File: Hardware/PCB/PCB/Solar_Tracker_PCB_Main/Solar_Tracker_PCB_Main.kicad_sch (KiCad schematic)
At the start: 1 part, among them J1 MTJ-88ARX1-FSM-LG

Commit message: Colocacion de los componentes en el PCB
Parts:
- removed J1: MTJ-88ARX1-FSM-LG, MTJ-88ARX1:MTJ88ARX1FSMLG, symbol MTJ-88ARX1-FSM-LG:MTJ-88ARX1-FSM-LG
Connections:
- no-connect marks 14 -> 0
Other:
- note removed: "RJ45 FEMALE"
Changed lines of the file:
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@@
 	(generator_version "9.0")
 	(paper "A4")
-	(rectangle
-		(start 236.22 12.7)
-		(end 284.48 59.69)
-		(stroke
-			(width 0)
-			(type default)
-		)
-		(fill
-			(type none)
-		)
-	)
-	(text "RJ45 FEMALE"
-		(exclude_from_sim no)
-		(at 260.35 20.32 0)
-		(effects
-			(font
-				(size 1.27 1.27)
-			)
-		)
-	)
-	(no_connect
-		(at 248.92 38.1)
-	)
-	(no_connect
-		(at 271.78 33.02)
-	)
-	(no_connect
-		(at 248.92 35.56)
-	)
-	(no_connect
-		(at 248.92 48.26)
-	)
-	(no_connect
-		(at 271.78 38.1)
-	)
-	(no_connect
-		(at 248.92 43.18)
-	)
-	(no_connect
-		(at 271.78 40.64)
-	)
-	(no_connect
-		(at 271.78 35.56)
-	)
-	(no_connect
-		(at 248.92 33.02)
-	)
-	(no_connect
-		(at 271.78 48.26)
-	)
-	(no_connect
-		(at 271.78 45.72)
-	)
-	(no_connect
-		(at 248.92 40.64)
-	)
-	(no_connect
-		(at 248.92 45.72)
-	)
-	(no_connect
-		(at 271.78 43.18)
-	)
-	(symbol
-		(lib_id "MTJ-88ARX1-FSM-LG:MTJ-88ARX1-FSM-LG")
-		(at 248.92 33.02 0)
-		(unit 1)
-		(exclude_from_sim no)
-		(in_bom yes)
-		(on_board yes)
-		(dnp no)
-		(fields_autoplaced yes)
-		(property "Reference" "J1"
-			(at 260.35 25.4 0)
-			(effects
-				(font
-					(size 1.27 1.27)
-				)
-			)
-		)
-		(property "Value" "MTJ-88ARX1-FSM-LG"
-			(at 260.35 27.94 0)
-			(effects
-				(font
-					(size 1.27 1.27)
-				)
-			)
-		)
-		(property "Footprint" "MTJ-88ARX1:MTJ88ARX1FSMLG"
-			(at 267.97 127.94 0)
-			(effects
-				(font
-					(size 1.27 1.27)
-				)
-				(justify left top)
-				(hide yes)
-			)
-		)
-		(property "Datasheet" "https://www.arrow.com/en/products/mtj-88arx1-fsm-lg/adam-tech"
-			(at 267.97 227.94 0)
-			(effects
-				(font
-					(size 1.27 1.27)
-				)
-				(justify left top)
-				(hide yes)
-			)
-		)
-		(property "Description" "RJ45 Modular Jack, Shielded, Dip, Side Entry,LEDs"
-			(at 248.92 33.02 0)
-			(effects
-				(font
-					(size 1.27 1.27)
-				)
-				(hide yes)
-			)
-		)
-		(property "Height" "13.708"
-			(at 267.97 427.94 0)
-			(effects
-				(font
-					(size 1.27 1.27)
-				)
-				(justify left top)
-				(hide yes)
-			)
-		)
-		(property "Mouser Part Number" "737-MTJ88ARX1FSMLG"
-			(at 267.97 527.94 0)
-			(effects
-				(font
-					(size 1.27 1.27)
-				)
-				(justify left top)
-				(hide yes)
-			)
-		)
-		(property "Mouser Price/Stock" "https://www.mouser.co.uk/ProductDetail/Adam-Tech/MTJ-88ARX1-FSM-LG?qs=HoCaDK9Nz5cwcndn7zcdzQ%3D%3D"
-			(at 267.97 627.94 0)
-			(effects
-				(font
-					(size 1.27 1.27)
-				)
-				(justify left top)
-				(hide yes)
-			)
-		)
-		(property "Manufacturer_Name" "Adam Tech"
-			(at 267.97 727.94 0)
-			(effects
-				(font
-					(size 1.27 1.27)
-				)
-				(justify left top)
-				(hide yes)
-			)
-		)
-		(property "Manufacturer_Part_Number" "MTJ-88ARX1-FSM-LG"
-			(at 267.97 827.94 0)
-			(effects
-				(font
-					(size 1.27 1.27)
-				)
-				(justify left top)
-				(hide yes)
-			)
-		)
-		(pin "11"
-		)
-		(pin "MH1"
-		)
-		(pin "MH2"
-		)
-		(pin "1"
-		)
-		(pin "4"
-		)
-		(pin "5"
-		)
-		(pin "8"
-		)
-		(pin "10"
-		)
-		(pin "6"
-		)
-		(pin "3"
-		)
-		(pin "7"
-		)
-		(pin "2"
-		)
-		(pin "9"
-		)
-		(pin "12"
-		)
-		(instances
-			(project ""
-				(path "/99b6ddd9-7ffe-4c85-972a-e0f594a166d4"
-					(reference "J1")
-					(unit 1)
-				)
-			)
-		)
-	)
 	(sheet
 		(at 17.78 21.59)

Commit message: Modificaciones PCB MAIN
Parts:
- added H1, H2, H3, H4: MountingHole_Pad, MountingHole:MountingHole_2.5mm_Pad, symbol Mechanical:MountingHole_Pad
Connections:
- new net GND: H1.1, H2.1, H3.1, H4.1

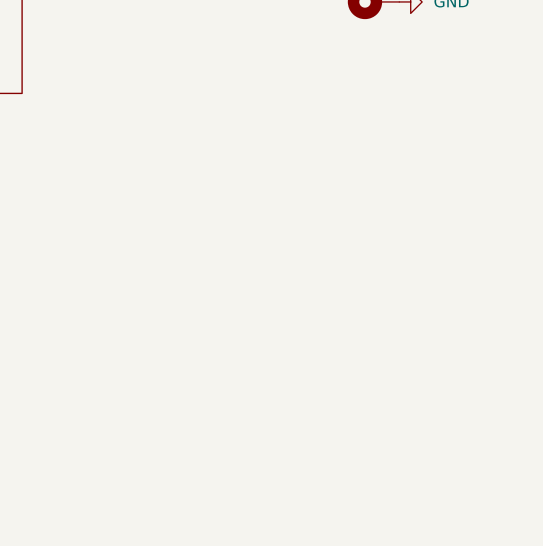
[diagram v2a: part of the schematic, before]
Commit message: Agregue pines vdd y gnd
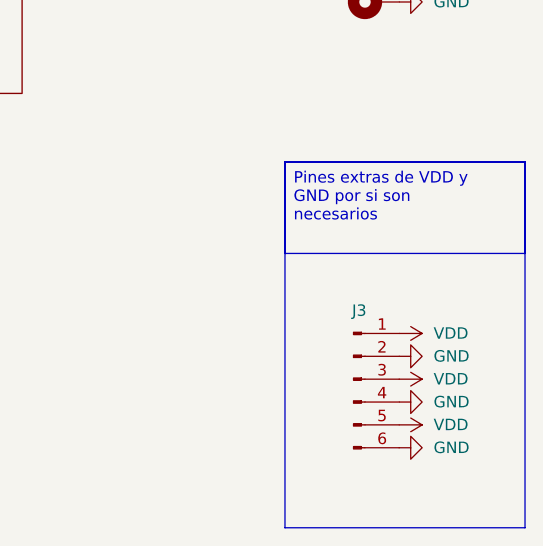
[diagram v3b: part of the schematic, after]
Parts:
- added J3: Conn_01x06_Pin, Connector_PinHeader_2.54mm:PinHeader_1x06_P2.54mm_Vertical, symbol Connector:Conn_01x06_Pin
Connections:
- net GND: now also J3.2 (Pin_2), J3.4 (Pin_4), J3.6 (Pin_6)
- new net VDD: J3.1 (Pin_1), J3.3 (Pin_3), J3.5 (Pin_5)
